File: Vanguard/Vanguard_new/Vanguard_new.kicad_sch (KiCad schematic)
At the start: 54 parts, among them J1 USB_B_Micro, J2 Conn_02x03_Pin, J3 Micro_SD_Card_Det1, Q1 BSS138, Q2 BSS138, Q3 BSS138, U1 ATSAMD11D14A-M, U2 ATmega4809-A, U3 BD1020HFV, U4 AP2112K-3.3, U5 MPM3610AGQV-P, U6 BNO086, U7 TXB0104D, Y1 32.768kHz

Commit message: added, flash mem
IMA KMS
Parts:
- removed U3: BD1020HFV, Package_TO_SOT_SMD:HVSOF5, symbol Sensor_Temperature:BD1020HFV
- added U3: AT25DF641A-SH-T, AT25DF641A-SH-T:SOIC127P798X216-8N, symbol AT25DF641A-SH-T:AT25DF641A-SH-T
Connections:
- net +3.3V: now also U2.14 (VCC), U2.28 (AVCC), U2.42 (VCC), U3.8 (VCC)
- net GND: now also U3.4 (GND)
- net PA0/MISO: now reaches U2.44 (PA0)
- net PA0/MISO: now also U3.2 (SO(SOI))
- net PA1/MOSI: now reaches U2.45 (PA1)
- net PA1/MOSI: now also U3.5 (SI(SIO))
- net PA2/SCK: now reaches U2.46 (PA2)
- net PA2/SCK: now also U3.6 (SCK)
- net PA3/SS: now reaches U2.47 (PA3)
- net PA3/SS: now also U3.1 (~{CS})
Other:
- note added: "FLASH CHIP"

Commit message: pin fix
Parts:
- J1: value USB_B_Micro -> USB_C
- renumbered ADR to ADR1
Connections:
- net SCL: now also U2.4 (PB0)
- net SDA: now also U2.48 (PA4)
- net UPDI: now also U2.41 (UPDI)
- net VBUS_out: now also U5.2 (VCC)
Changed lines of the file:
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@@
 	)
 	(global_label "SDA"
-		(shape input)
+		(shape bidirectional)
 		(at 49.53 148.59 180)
 		(fields_autoplaced yes)
@@
 		)
 		(property "Intersheetrefs" "${INTERSHEET_REFS}"
-			(at 42.9767 148.59 0)
+			(at 41.8654 148.59 0)
 			(effects
 				(font
@@
 		)
 	)
+	(global_label "VBUS_out"
+		(shape input)
+		(at 290.83 58.42 180)
+		(fields_autoplaced yes)
+		(effects
+			(font
+				(size 1.27 1.27)
+			)
+			(justify right)
+		)
+		(property "Intersheetrefs" "${INTERSHEET_REFS}"
+			(at 278.9549 58.42 0)
+			(effects
+				(font
+					(size 1.27 1.27)
+				)
+				(justify right)
+				(hide yes)
+			)
+		)
+	)
 	(global_label "RST"
 		(shape input)
@@
 		)
 	)
+	(global_label "UPDI"
+		(shape input)
+		(at 368.3 163.83 0)
+		(fields_autoplaced yes)
+		(effects
+			(font
+				(size 1.27 1.27)
+			)
+			(justify left)
+		)
+		(property "Intersheetrefs" "${INTERSHEET_REFS}"
+			(at 375.7605 163.83 0)
+			(effects
+				(font
+					(size 1.27 1.27)
+				)
+				(justify left)
+				(hide yes)
+			)
+		)
+	)
 	(global_label "PA3{slash}SS"
 		(shape passive)
@@
 		)
 	)
+	(global_label "SCL"
+		(shape input)
+		(at 337.82 140.97 180)
+		(fields_autoplaced yes)
+		(effects
+			(font
+				(size 1.27 1.27)
+			)
+			(justify right)
+		)
+		(property "Intersheetrefs" "${INTERSHEET_REFS}"
+			(at 331.3272 140.97 0)
+			(effects
+				(font
+					(size 1.27 1.27)
+				)
+				(justify right)
+				(hide yes)
+			)
+		)
+	)
 	(global_label "CD"
 		(shape input)
@@
 		)
 	)
+	(global_label "SDA"
+		(shape bidirectional)
+		(at 337.82 153.67 180)
+		(fields_autoplaced yes)
+		(effects
+			(font
+				(size 1.27 1.27)
+			)
+			(justify right)
+		)
+		(property "Intersheetrefs" "${INTERSHEET_REFS}"
+			(at 330.1554 153.67 0)
+			(effects
+				(font
+					(size 1.27 1.27)
+				)
+				(justify right)
+				(hide yes)
+			)
+		)
+	)
 	(global_label "PA2{slash}SCK"
 		(shape input)
@@
 			)
 		)
-		(property "Value" "USB_B_Micro"
+		(property "Value" "USB_C"
 			(at 35.56 17.78 0)
 			(effects
@@
 		(on_board yes)
 		(dnp no)
-		(fields_autoplaced yes)
 		(property "Reference" "#PWR025"
 			(at 280.67 58.42 0)
@@
 		)
 		(property "Value" "GND"
-			(at 280.67 57.15 0)
+			(at 276.098 51.562 0)
 			(effects
 				(font
@@
 		(on_board yes)
 		(dnp no)
-		(property "Reference" "ADR"
+		(property "Reference" "ADR1"
 			(at 32.258 147.828 0)
 			(effects
@@
 			(project ""
 				(path "/972fbf12-2dcd-4fdf-b1c9-8a2880c46640"
-					(reference "ADR")
+					(reference "ADR1")
 					(unit 1)
 				)

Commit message: start of pcb layout
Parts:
- ADR1: footprint (none) -> Jumper:SolderJumper-2_P1.3mm_Bridged2Bar_Pad1.0x1.5mm
- C1, C2, C3, C4, C5, C6, C7: footprint (none) -> Capacitor_SMD:C_0201_0603Metric
- D2, D3, D5: footprint (none) -> LED_SMD:LED_0201_0603Metric
- D4: now not fitted
- J1: footprint (none) -> Connector_USB:USB_C_Plug_Molex_105444
- J2: footprint (none) -> Connector_PinSocket_2.54mm:PinSocket_2x03_P2.54mm_Vertical
- J3: footprint (none) -> Connector_Card:microSD_HC_Molex_104031-0811
- R1, R10, R11, R12, R13, R14, R15, R16, R17, R18, R19, R2, R20, R21, R22, R23, R24, R3, R4, R5, R6, R7, R8, R9: footprint (none) -> Resistor_SMD:R_0402_1005Metric
- TP1, TP2: footprint (none) -> TestPoint:TestPoint_2Pads_Pitch5.08mm_Drill1.3mm
- U5: footprint MPM3610AGQV-P:CONV_MPM3620AGQV-P -> MPM3610AGQV_P:CONV_MPM3620AGQV-P
- Y1: footprint (none) -> Crystal:Crystal_C26-LF_D2.1mm_L6.5mm_Vertical
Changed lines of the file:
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@@
 			)
 		)
-		(property "Footprint" ""
+		(property "Footprint" "Resistor_SMD:R_0402_1005Metric"
 			(at 118.11 163.068 90)
 			(effects
@@
 			)
 		)
-		(property "Footprint" ""
+		(property "Footprint" "Capacitor_SMD:C_0201_0603Metric"
 			(at 53.0352 62.23 0)
 			(effects
@@
 			)
 		)
-		(property "Footprint" ""
+		(property "Footprint" "Resistor_SMD:R_0402_1005Metric"
 			(at 203.962 50.8 90)
 			(effects
@@
 			)
 		)
-		(property "Footprint" ""
+		(property "Footprint" "Resistor_SMD:R_0402_1005Metric"
 			(at 114.3 34.798 90)
 			(effects
@@
 			)
 		)
-		(property "Footprint" ""
+		(property "Footprint" "Capacitor_SMD:C_0201_0603Metric"
 			(at 139.7 150.1648 0)
 			(effects
@@
 			)
 		)
-		(property "Footprint" ""
+		(property "Footprint" "Resistor_SMD:R_0402_1005Metric"
 			(at 167.64 50.038 90)
 			(effects
@@
 			)
 		)
-		(property "Footprint" ""
+		(property "Footprint" "Resistor_SMD:R_0402_1005Metric"
 			(at 60.452 135.89 90)
 			(effects
@@
 			)
 		)
-		(property "Footprint" ""
+		(property "Footprint" "Capacitor_SMD:C_0201_0603Metric"
 			(at 281.6352 52.07 0)
 			(effects
@@
 			)
 		)
-		(property "Footprint" ""
+		(property "Footprint" "Resistor_SMD:R_0402_1005Metric"
 			(at 153.67 160.528 90)
 			(effects
@@
 			)
 		)
-		(property "Footprint" ""
+		(property "Footprint" "Capacitor_SMD:C_0201_0603Metric"
 			(at 121.92 165.4048 0)
 			(effects
@@
 			)
 		)
-		(property "Footprint" ""
+		(property "Footprint" "Resistor_SMD:R_0402_1005Metric"
 			(at 153.67 156.718 90)
 			(effects
@@
 			)
 		)
-		(property "Footprint" ""
+		(property "Footprint" "Resistor_SMD:R_0402_1005Metric"
 			(at 254.762 53.34 90)
 			(effects
@@
 			)
 		)
-		(property "Footprint" ""
+		(property "Footprint" "Resistor_SMD:R_0402_1005Metric"
 			(at 61.722 58.42 90)
 			(effects
@@
 			)
 		)
-		(property "Footprint" ""
+		(property "Footprint" "Crystal:Crystal_C26-LF_D2.1mm_L6.5mm_Vertical"
 			(at 119.38 147.32 0)
 			(effects
@@
 			)
 		)
-		(property "Footprint" ""
+		(property "Footprint" "Resistor_SMD:R_0402_1005Metric"
 			(at 186.182 35.56 90)
 			(effects
@@
 			)
 		)
-		(property "Footprint" ""
+		(property "Footprint" "Resistor_SMD:R_0402_1005Metric"
 			(at 181.61 53.848 90)
 			(effects
@@
 			)
 		)
-		(property "Footprint" ""
+		(property "Footprint" "Resistor_SMD:R_0402_1005Metric"
 			(at 282.702 40.64 90)
 			(effects
@@
 			)
 		)
-		(property "Footprint" ""
+		(property "Footprint" "Resistor_SMD:R_0402_1005Metric"
 			(at 327.152 60.96 90)
 			(effects
@@
 			)
 		)
-		(property "Footprint" ""
+		(property "Footprint" "LED_SMD:LED_0201_0603Metric"
 			(at 166.37 74.93 0)
 			(effects
@@
 		(in_bom yes)
 		(on_board yes)
-		(dnp no)
+		(dnp yes)
 		(fields_autoplaced yes)
 		(property "Reference" "D4"
@@
 			)
 		)
-		(property "Footprint" ""
+		(property "Footprint" "TestPoint:TestPoint_2Pads_Pitch5.08mm_Drill1.3mm"
 			(at 59.69 41.91 0)
 			(effects
@@
 			)
 		)
-		(property "Footprint" ""
+		(property "Footprint" "Resistor_SMD:R_0402_1005Metric"
 			(at 58.42 157.988 90)
 			(effects
@@
 			)
 		)
-		(property "Footprint" ""
+		(property "Footprint" "Resistor_SMD:R_0402_1005Metric"
 			(at 327.152 48.26 90)
 			(effects
@@
 			)
 		)
-		(property "Footprint" ""
+		(property "Footprint" "Capacitor_SMD:C_0201_0603Metric"
 			(at 374.3452 52.07 0)
 			(effects
@@
 			)
 		)
-		(property "Footprint" ""
+		(property "Footprint" "Connector_Card:microSD_HC_Molex_104031-0811"
 			(at 147.32 252.73 0)
 			(effects
@@
 			)
 		)
-		(property "Footprint" ""
+		(property "Footprint" "Capacitor_SMD:C_0201_0603Metric"
 			(at 147.32 142.5448 0)
 			(effects
@@
 			)
 		)
-		(property "Footprint" ""
+		(property "Footprint" "Resistor_SMD:R_0402_1005Metric"
 			(at 27.432 140.97 90)
 			(effects
@@
 			)
 		)
-		(property "Footprint" ""
+		(property "Footprint" "Resistor_SMD:R_0402_1005Metric"
 			(at 114.3 39.878 90)
 			(effects
@@
 			)
 		)
-		(property "Footprint" ""
+		(property "Footprint" "LED_SMD:LED_0201_0603Metric"
 			(at 384.81 55.88 0)
 			(effects
@@
 			)
 		)
-		(property "Footprint" ""
+		(property "Footprint" "TestPoint:TestPoint_2Pads_Pitch5.08mm_Drill1.3mm"
 			(at 97.79 26.67 0)
 			(effects
@@
 			)
 		)
-		(property "Footprint" ""
+		(property "Footprint" "Resistor_SMD:R_0402_1005Metric"
 			(at 238.252 53.34 90)
 			(effects
@@
 			)
 		)
-		(property "Footprint" ""
+		(property "Footprint" "Resistor_SMD:R_0402_1005Metric"
 			(at 220.472 50.8 90)
 			(effects
@@
 			)
 		)
-		(property "Footprint" ""
+		(property "Footprint" "Resistor_SMD:R_0402_1005Metric"
 			(at 168.148 82.55 90)
 			(effects
@@
 			)
 		)
-		(property "Footprint" ""
+		(property "Footprint" "Connector_USB:USB_C_Plug_Molex_105444"
 			(at 39.37 38.1 0)
 			(effects
@@
 			)
 		)
-		(property "Footprint" ""
+		(property "Footprint" "Resistor_SMD:R_0402_1005Metric"
 			(at 160.528 82.55 90)
 			(effects
@@
 			)
 		)
-		(property "Footprint" ""
+		(property "Footprint" "Resistor_SMD:R_0402_1005Metric"
 			(at 50.292 135.89 90)
 			(effects
@@
 			)
 		)
-		(property "Footprint" ""
+		(property "Footprint" "LED_SMD:LED_0201_0603Metric"
 			(at 158.75 74.93 0)
 			(effects
@@
 			)
 		)
-		(property "Footprint" ""
+		(property "Footprint" "Capacitor_SMD:C_0201_0603Metric"
 			(at 342.5952 52.07 0)
 			(effects
@@
 			)
 		)
-		(property "Footprint" ""
+		(property "Footprint" "Jumper:SolderJumper-2_P1.3mm_Bridged2Bar_Pad1.0x1.5mm"
 			(at 29.21 149.86 0)
 			(effects
@@
 			)
 		)
-		(property "Footprint" ""
+		(property "Footprint" "Connector_PinSocket_2.54mm:PinSocket_2x03_P2.54mm_Vertical"
 			(at 101.6 60.96 0)
 			(effects
@@
 			)
 		)
-		(property "Footprint" ""
+		(property "Footprint" "Resistor_SMD:R_0402_1005Metric"
 			(at 383.032 48.26 90)
 			(effects
@@
 			)
 		)
-		(property "Footprint" ""
+		(property "Footprint" "Resistor_SMD:R_0402_1005Metric"
 			(at 169.672 35.56 90)
 			(effects
@@
 			)
 		)
-		(property "Footprint" "MPM3610AGQV-P:CONV_MPM3620AGQV-P"
+		(property "Footprint" "MPM3610AGQV_P:CONV_MPM3620AGQV-P"
 			(at 306.07 46.99 0)
 			(effects

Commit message: schematic with leds and servos
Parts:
- added C10: 100 uF, symbol Device:C_Polarized_US
- added C8: 10 uF, symbol Device:C
- added C9: 2.2uF, symbol Device:C
- added J4: STARBOARD_SERVO, symbol Connector:Conn_01x03_Pin
- added J5: PORTSIDE_SERVO, symbol Connector:Conn_01x03_Pin
- added J6: LIPO_in, symbol Connector:Screw_Terminal_01x02
- added L1: 6.8 uH, symbol Device:L
- added PORTSIDE_RGB, STARBOARD_RGB: SMLVN6RGB, LED_SMD:LED_ROHM_SMLVN6, symbol LED:SMLVN6RGB
- added R25, R26, R27, R28, R29, R30: 220, symbol Device:R
- added U8: TPS61092, Package_DFN_QFN:Texas_RSA_VQFN-16-1EP_4x4mm_P0.65mm_EP2.7x2.7mm_ThermalVias, symbol Regulator_Switching:TPS61092
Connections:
- net GND: now also C10.2, C8.2, C9.2, J4.3 (Pin_3), J5.3 (Pin_3), J6.1 (Pin_1), PORTSIDE_RGB.4 (GK), PORTSIDE_RGB.5 (RK), PORTSIDE_RGB.6 (BK), STARBOARD_RGB.4 (GK), STARBOARD_RGB.5 (RK), STARBOARD_RGB.6 (BK), U8.10 (SYNC), U8.13 (GND), U8.3 (SW), U8.5 (PGND), U8.6 (PGND), U8.7 (PGND)
- net STAR_RED: now reaches U2.10 (PC0)
- net STAR_RED: now also R26.1
- net STAR_GREEN: now reaches U2.11 (PC1)
- net STAR_GREEN: now also R27.1
- net STAR_BLUE: now reaches U2.12 (PC2)
- net STAR_BLUE: now also R25.1
- net PORT_SERVO: now reaches U2.13 (PC3)
- net PORT_SERVO: now also J5.1 (Pin_1)
- net PORT_RED: now reaches U2.30 (PE0)
- net PORT_RED: now also R29.2
- net PORT_GREEN: now reaches U2.34 (PF0)
- net PORT_GREEN: now also R30.2
- net PORT_BLUE: now reaches U2.35 (PF1)
- net PORT_BLUE: now also R28.2
- net STAR_SERVO: now reaches U2.36 (PF2)
- net STAR_SERVO: now also J4.1 (Pin_1)
- net VBUS_out renamed VCC
- net VCC: now also C8.1, J6.2 (Pin_2), L1.1, U8.11 (EN), U8.8 (VBAT)
- new net: R25.2, STARBOARD_RGB.1 (BA)
- new net: PORTSIDE_RGB.3 (GA), R30.1
- new net: R26.2, STARBOARD_RGB.2 (RA)
- new net: R27.2, STARBOARD_RGB.3 (GA)
- new net: L1.2, U8.4 (SW)
- new net: PORTSIDE_RGB.1 (BA), R28.1
- new net: PORTSIDE_RGB.2 (RA), R29.1
- new net +5V: C10.1, C9.1, J4.2 (Pin_2), J5.2 (Pin_2), U8.1 (VOUT)
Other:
- note added: "LEDS"
- note added: "SERVO POWER"
- note added: "SERVOS"
- moved on the sheet: U2, U3

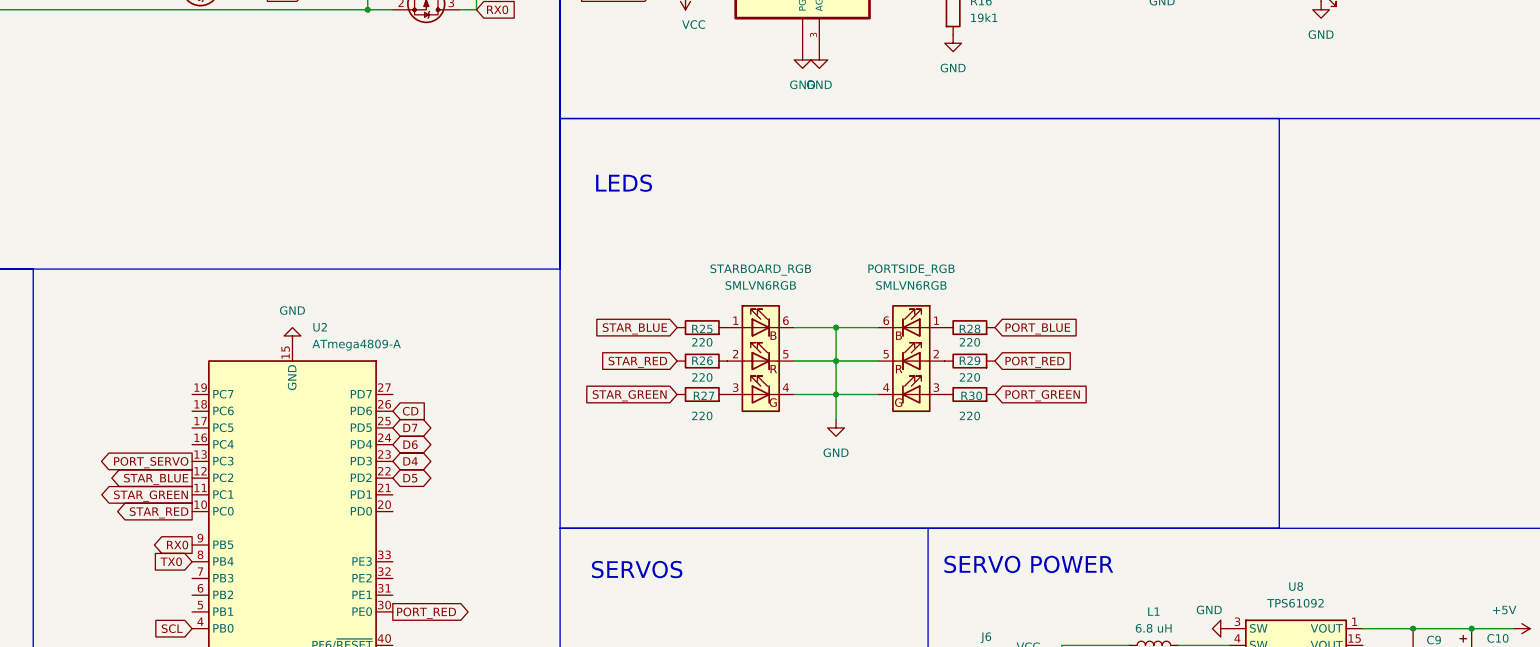
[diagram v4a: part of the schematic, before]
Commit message: buzzer added
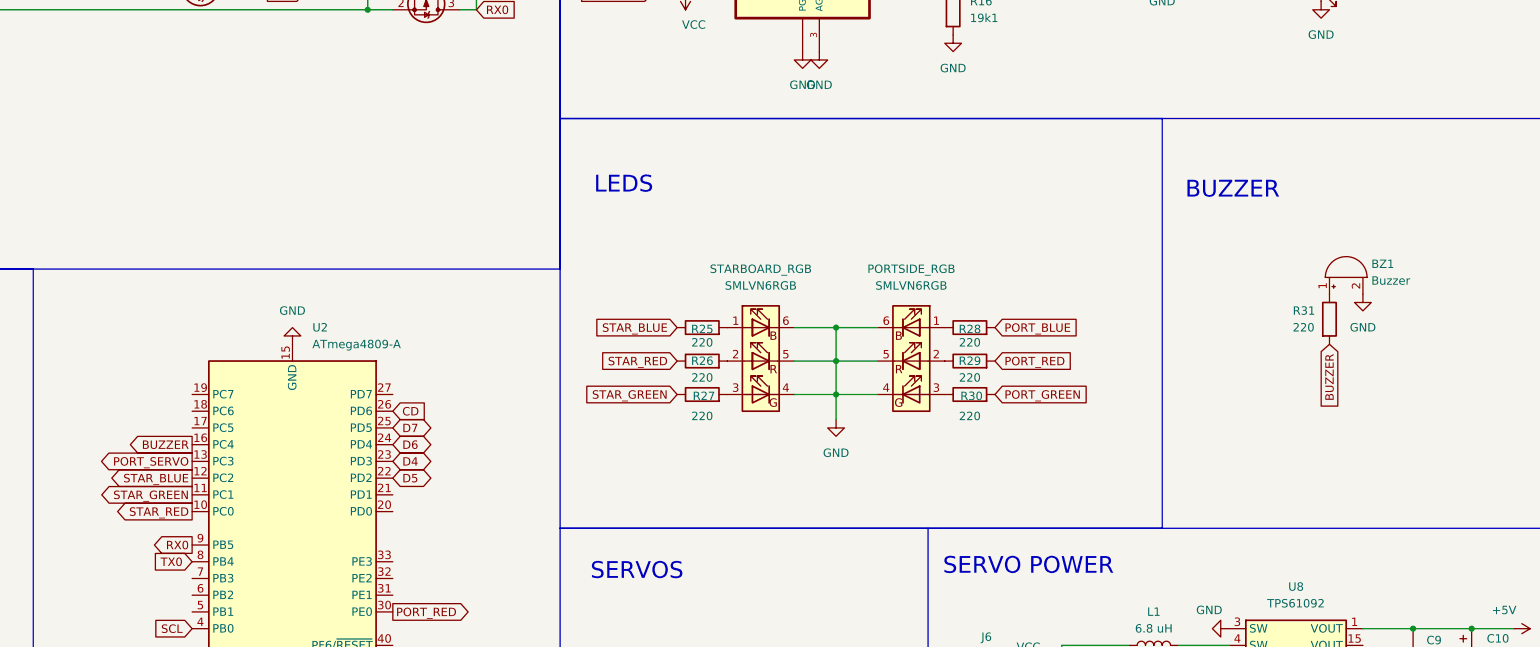
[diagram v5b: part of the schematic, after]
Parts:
- added BZ1: Buzzer, symbol Device:Buzzer
- added R31: 220, symbol Device:R
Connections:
- net GND: now also BZ1.2 (-)
- net BUZZER: now reaches U2.16 (PC4)
- net BUZZER: now also R31.2
- new net: BZ1.1 (+), R31.1
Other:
- note added: "BUZZER"
